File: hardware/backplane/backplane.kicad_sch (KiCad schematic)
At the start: 83 parts, among them J1 Bus_PCI_Express_x1, J2 PWR, J3 Bus_PCI_Express_x1, J4 Bus_PCI_Express_x1, J5 Bus_PCI_Express_x1, J6 Bus_PCI_Express_x1, J7 Bus_PCI_Express_x1, J8 Bus_PCI_Express_x1, M1 FAN1, Q1 IRFS7530TRL7PP, Q2 AO3400A, U1 TPS5430DDA, U2 TCA9548APWR, U3 TCA9539PWR, U4 LM74700

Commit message: chore: clean up socket definitions
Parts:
- J1, J3, J4, J5, J6, J7, J8: LCSC (none) -> C4693418; now not fitted
- U3: LCSC (none) -> C131972
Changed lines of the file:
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@@
 			)
 		)
+		(property "LCSC" "C131972"
+			(at 134.62 234.95 0)
+			(hide yes)
+			(show_name no)
+			(do_not_autoplace no)
+			(effects
+				(font
+					(size 1.27 1.27)
+				)
+			)
+		)
 		(pin "16"
 		)
@@
 		(on_board yes)
 		(in_pos_files yes)
-		(dnp no)
+		(dnp yes)
 		(fields_autoplaced yes)
 		(property "Reference" "J8"
@@
 			)
 		)
+		(property "LCSC" "C4693418"
+			(at 331.47 191.77 0)
+			(hide yes)
+			(show_name no)
+			(do_not_autoplace no)
+			(effects
+				(font
+					(size 1.27 1.27)
+				)
+			)
+		)
 		(pin "A10"
 		)
@@
 		(on_board yes)
 		(in_pos_files yes)
-		(dnp no)
+		(dnp yes)
 		(fields_autoplaced yes)
 		(property "Reference" "J1"
@@
 			)
 		)
+		(property "LCSC" "C4693418"
+			(at 62.23 166.37 0)
+			(hide yes)
+			(show_name no)
+			(do_not_autoplace no)
+			(effects
+				(font
+					(size 1.27 1.27)
+				)
+			)
+		)
 		(pin "A10"
 		)
@@
 		(on_board yes)
 		(in_pos_files yes)
-		(dnp no)
+		(dnp yes)
 		(fields_autoplaced yes)
 		(property "Reference" "J5"
@@
 			)
 		)
+		(property "LCSC" "C4693418"
+			(at 274.32 113.03 0)
+			(hide yes)
+			(show_name no)
+			(do_not_autoplace no)
+			(effects
+				(font
+					(size 1.27 1.27)
+				)
+			)
+		)
 		(pin "A10"
 		)
@@
 		(on_board yes)
 		(in_pos_files yes)
-		(dnp no)
+		(dnp yes)
 		(fields_autoplaced yes)
 		(property "Reference" "J7"
@@
 			)
 		)
+		(property "LCSC" "C4693418"
+			(at 331.47 114.3 0)
+			(hide yes)
+			(show_name no)
+			(do_not_autoplace no)
+			(effects
+				(font
+					(size 1.27 1.27)
+				)
+			)
+		)
 		(pin "A10"
 		)
@@
 		(on_board yes)
 		(in_pos_files yes)
-		(dnp no)
+		(dnp yes)
 		(fields_autoplaced yes)
 		(property "Reference" "J3"
@@
 			)
 		)
-		(property "Manufacturer_Name" ""
-			(at 217.17 111.76 0)
-			(hide yes)
-			(show_name no)
-			(do_not_autoplace no)
-			(effects
-				(font
-					(size 1.27 1.27)
-				)
-			)
-		)
-		(property "Manufacturer_Part_Number" ""
-			(at 217.17 111.76 0)
-			(hide yes)
-			(show_name no)
-			(do_not_autoplace no)
-			(effects
-				(font
-					(size 1.27 1.27)
-				)
-			)
-		)
-		(property "Mouser Part Number" ""
-			(at 217.17 111.76 0)
-			(hide yes)
-			(show_name no)
-			(do_not_autoplace no)
-			(effects
-				(font
-					(size 1.27 1.27)
-				)
-			)
-		)
-		(property "Mouser Price/Stock" ""
+		(property "LCSC" "C4693418"
 			(at 217.17 111.76 0)
 			(hide yes)
@@
 		(on_board yes)
 		(in_pos_files yes)
-		(dnp no)
+		(dnp yes)
 		(fields_autoplaced yes)
 		(property "Reference" "J4"
@@
 			)
 		)
+		(property "LCSC" "C4693418"
+			(at 217.17 189.23 0)
+			(hide yes)
+			(show_name no)
+			(do_not_autoplace no)
+			(effects
+				(font
+					(size 1.27 1.27)
+				)
+			)
+		)
 		(pin "A10"
 		)
@@
 		(on_board yes)
 		(in_pos_files yes)
-		(dnp no)
+		(dnp yes)
 		(fields_autoplaced yes)
 		(property "Reference" "J6"
@@
 			(at 274.32 190.5 0)
 			(hide yes)
+			(show_name no)
+			(do_not_autoplace no)
+			(effects
+				(font
+					(size 1.27 1.27)
+				)
+			)
+		)
+		(property "LCSC" "C4693418"
+			(at 274.32 190.5 0)
+			(hide yes)

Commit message: chore: remove DNP from sockets
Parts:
- J1, J3, J4, J5, J6, J7, J8: now fitted
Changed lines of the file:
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@@
 		(on_board yes)
 		(in_pos_files yes)
-		(dnp yes)
+		(dnp no)
 		(fields_autoplaced yes)
 		(property "Reference" "J8"
@@
 		(on_board yes)
 		(in_pos_files yes)
-		(dnp yes)
+		(dnp no)
 		(fields_autoplaced yes)
 		(property "Reference" "J1"
@@
 		(on_board yes)
 		(in_pos_files yes)
-		(dnp yes)
+		(dnp no)
 		(fields_autoplaced yes)
 		(property "Reference" "J5"
@@
 		(on_board yes)
 		(in_pos_files yes)
-		(dnp yes)
+		(dnp no)
 		(fields_autoplaced yes)
 		(property "Reference" "J7"
@@
 		(on_board yes)
 		(in_pos_files yes)
-		(dnp yes)
+		(dnp no)
 		(fields_autoplaced yes)
 		(property "Reference" "J3"
@@
 		(on_board yes)
 		(in_pos_files yes)
-		(dnp yes)
+		(dnp no)
 		(fields_autoplaced yes)
 		(property "Reference" "J4"
@@
 		(on_board yes)
 		(in_pos_files yes)
-		(dnp yes)
+		(dnp no)
 		(fields_autoplaced yes)
 		(property "Reference" "J6"

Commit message: chore(backplane): fix 3d models
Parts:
- D10, D5, D6, D7, D8, D9: footprint LED_SMD:LED_WS2812B-2020_PLCC4_2.0x2.0mm -> Local Library:LED_WS2812B-2020_PLCC4_2.0x2.0mm
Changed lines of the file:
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@@
 			)
 		)
-		(property "Footprint" "LED_SMD:LED_WS2812B-2020_PLCC4_2.0x2.0mm"
+		(property "Footprint" "Local Library:LED_WS2812B-2020_PLCC4_2.0x2.0mm"
 			(at 375.92 73.66 0)
 			(hide yes)
@@
 			)
 		)
-		(property "Footprint" "LED_SMD:LED_WS2812B-2020_PLCC4_2.0x2.0mm"
+		(property "Footprint" "Local Library:LED_WS2812B-2020_PLCC4_2.0x2.0mm"
 			(at 375.92 58.42 0)
 			(hide yes)
@@
 		(in_bom no)
 		(on_board yes)
-		(in_pos_files yes)
+		(in_pos_files no)
 		(dnp no)
 		(property "Reference" "F1"
@@
 			)
 		)
-		(property "Footprint" "LED_SMD:LED_WS2812B-2020_PLCC4_2.0x2.0mm"
+		(property "Footprint" "Local Library:LED_WS2812B-2020_PLCC4_2.0x2.0mm"
 			(at 375.92 134.62 0)
 			(hide yes)
@@
 			)
 		)
-		(property "Footprint" "LED_SMD:LED_WS2812B-2020_PLCC4_2.0x2.0mm"
+		(property "Footprint" "Local Library:LED_WS2812B-2020_PLCC4_2.0x2.0mm"
 			(at 375.92 119.38 0)
 			(hide yes)
@@
 		(in_bom no)
 		(on_board yes)
-		(in_pos_files yes)
+		(in_pos_files no)
 		(dnp no)
 		(property "Reference" "H1"
@@
 			)
 		)
-		(property "Footprint" "LED_SMD:LED_WS2812B-2020_PLCC4_2.0x2.0mm"
+		(property "Footprint" "Local Library:LED_WS2812B-2020_PLCC4_2.0x2.0mm"
 			(at 375.92 104.14 0)
 			(hide yes)
@@
 			)
 		)
-		(property "Footprint" "LED_SMD:LED_WS2812B-2020_PLCC4_2.0x2.0mm"
+		(property "Footprint" "Local Library:LED_WS2812B-2020_PLCC4_2.0x2.0mm"
 			(at 375.92 88.9 0)
 			(hide yes)
@@
 		(in_bom no)
 		(on_board yes)
-		(in_pos_files yes)
+		(in_pos_files no)
 		(dnp no)
 		(fields_autoplaced yes)

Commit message: chore: assembly cleanup
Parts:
- D10, D5, D6, D7, D8, D9: value WS2812C-2020 -> WS2812C-2020-V6
- J2: JLCPCB_CORRECTION (none) -> 3;1.5;180
- Q1: JLCPCB_CORRECTION -2.5;0;0 -> (none)
- Q2: JLCPCB_CORRECTION (none) -> 0;0;180
- RN1, RN2, RN3, RN4, RN5, RN6, RN7, RN8: JLCPCB_CORRECTION (none) -> 0;0;90
- U3, U4: JLCPCB_CORRECTION (none) -> 0;0;270
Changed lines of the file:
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@@
 			)
 		)
+		(property "JLCPCB_CORRECTION" "0;0;270"
+			(at 134.62 234.95 0)
+			(hide yes)
+			(show_name no)
+			(do_not_autoplace no)
+			(effects
+				(font
+					(size 1.27 1.27)
+				)
+			)
+		)
 		(pin "16"
 		)
@@
 			)
 		)
+		(property "JLCPCB_CORRECTION" "0;0;90"
+			(at 157.48 219.71 90)
+			(hide yes)
+			(show_name no)
+			(do_not_autoplace no)
+			(effects
+				(font
+					(size 1.27 1.27)
+				)
+			)
+		)
 		(pin "7"
 		)
@@
 			)
 		)
-		(property "Value" "WS2812C-2020"
+		(property "Value" "WS2812C-2020-V6"
 			(at 397.51 68.5098 90)
 			(show_name no)
@@
 			)
 		)
-		(property "Value" "WS2812C-2020"
+		(property "Value" "WS2812C-2020-V6"
 			(at 397.51 53.2698 90)
 			(show_name no)
@@
 			)
 		)
+		(property "JLCPCB_CORRECTION" "0;0;270"
+			(at 142.24 48.26 0)
+			(hide yes)
+			(show_name no)
+			(do_not_autoplace no)
+			(effects
+				(font
+					(size 1.27 1.27)
+				)
+			)
+		)
 		(pin "1"
 		)
@@
 			)
 		)
+		(property "JLCPCB_CORRECTION" "0;0;90"
+			(at 59.69 254 90)
+			(hide yes)
+			(show_name no)
+			(do_not_autoplace no)
+			(effects
+				(font
+					(size 1.27 1.27)
+				)
+			)
+		)
 		(pin "7"
 		)
@@
 			)
 		)
+		(property "JLCPCB_CORRECTION" "0;0;90"
+			(at 59.69 218.44 90)
+			(hide yes)
+			(show_name no)
+			(do_not_autoplace no)
+			(effects
+				(font
+					(size 1.27 1.27)
+				)
+			)
+		)
 		(pin "7"
 		)
@@
 			)
 		)
-		(property "JLCPCB_CORRECTION" "-2.5;0;0"
+		(property "JLCPCB_CORRECTION" ""
 			(at 142.24 31.75 90)
 			(hide yes)
@@
 			)
 		)
+		(property "JLCPCB_CORRECTION" "0;0;90"
+			(at 59.69 241.3 90)
+			(hide yes)
+			(show_name no)
+			(do_not_autoplace no)
+			(effects
+				(font
+					(size 1.27 1.27)
+				)
+			)
+		)
 		(pin "7"
 		)
@@
 			)
 		)
+		(property "JLCPCB_CORRECTION" "0;0;180"
+			(at 194.31 45.72 0)
+			(hide yes)
+			(show_name no)
+			(do_not_autoplace no)
+			(effects
+				(font
+					(size 1.27 1.27)
+				)
+			)
+		)
 		(pin "1"
 		)
@@
 			)
 		)
-		(property "Value" "WS2812C-2020"
+		(property "Value" "WS2812C-2020-V6"
 			(at 397.51 129.4698 90)
 			(show_name no)
@@
 			)
 		)
-		(property "Value" "WS2812C-2020"
+		(property "Value" "WS2812C-2020-V6"
 			(at 397.51 114.2298 90)
 			(show_name no)
@@
 			)
 		)
+		(property "JLCPCB_CORRECTION" "0;0;90"
+			(at 157.48 242.57 90)
+			(hide yes)
+			(show_name no)
+			(do_not_autoplace no)
+			(effects
+				(font
+					(size 1.27 1.27)
+				)
+			)
+		)
 		(pin "7"
 		)
@@
 			)
 		)
-		(property "Value" "WS2812C-2020"
+		(property "Value" "WS2812C-2020-V6"
 			(at 397.51 98.9898 90)
 			(show_name no)
@@
 			)
 		)
+		(property "JLCPCB_CORRECTION" "0;0;90"
+			(at 59.69 228.6 90)
+			(hide yes)
+			(show_name no)
+			(do_not_autoplace no)
+			(effects
+				(font
+					(size 1.27 1.27)
+				)
+			)
+		)
 		(pin "7"
 		)
@@
 			)
 		)
+		(property "JLCPCB_CORRECTION" "0;0;90"
+			(at 157.48 252.73 90)
+			(hide yes)
+			(show_name no)
+			(do_not_autoplace no)
+			(effects
+				(font
+					(size 1.27 1.27)
+				)
+			)
+		)
 		(pin "7"
 		)
@@
 			)
 		)
+		(property "JLCPCB_CORRECTION" "0;0;90"
+			(at 157.48 229.87 90)
+			(hide yes)
+			(show_name no)
+			(do_not_autoplace no)
+			(effects
+				(font
+					(size 1.27 1.27)
+				)
+			)
+		)
 		(pin "7"
 		)
@@
 			)
 		)
-		(property "Value" "WS2812C-2020"
+		(property "Value" "WS2812C-2020-V6"
 			(at 397.51 83.7498 90)
 			(show_name no)
@@
 			(at 78.74 36.83 90)
 			(hide yes)
+			(show_name no)
+			(do_not_autoplace no)
+			(effects
+				(font
+					(size 1.27 1.27)
+				)
+			)
+		)
+		(property "JLCPCB_CORRECTION" "3;1.5;180"
+			(at 78.74 36.83 90)
+			(hide yes)

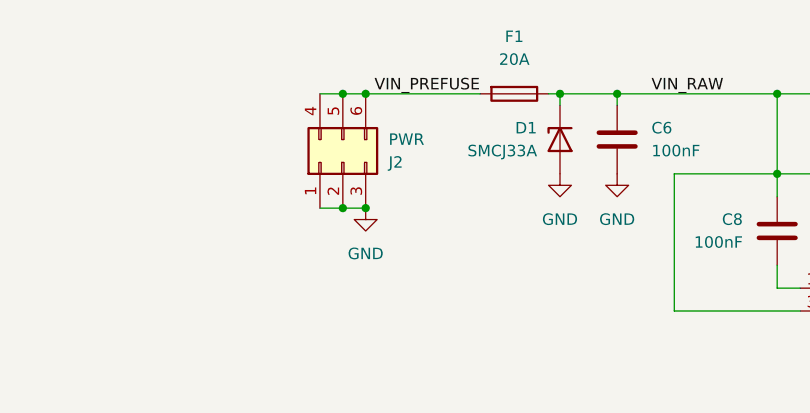
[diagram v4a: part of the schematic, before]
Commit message: feat(backplane): update pcb for higher power
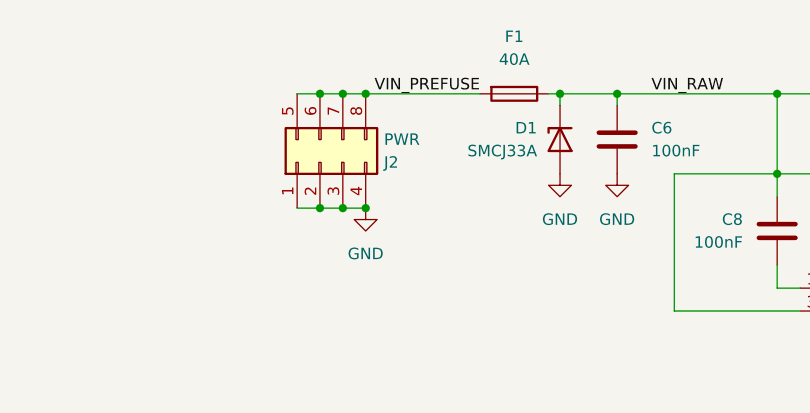
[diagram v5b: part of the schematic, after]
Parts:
- F1: value 20A -> 40A; footprint Local Library:Fuseholder_Blade_Mini_Keystone_3568 -> Local Library:FuseHolder_Blade_ATO_Littelfuse_FLR_178.6165
- J2: footprint Local Library:Molex_Micro-Fit_3.0_43045-0600_2x03_P3.00mm_Horizontal -> Local Library:Molex_Micro-Fit_3.0_43045-0812_2x04_P3.00mm_Vertical; symbol Connector_Generic:Conn_02x03_Top_Bottom -> Connector_Generic:Conn_02x04_Top_Bottom; JLCPCB_CORRECTION 3;1.5;180 -> 0;0;0; LCSC C3294384 -> C505221
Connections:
- net GND: now also J2.4 (Pin_4)
- net VIN_PREFUSE: now also J2.7 (Pin_7), J2.8 (Pin_8); no longer J2.4 (Pin_4)
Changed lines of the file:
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@@
 	)
 	(junction
-		(at 78.74 29.21)
+		(at 220.98 154.94)
 		(diameter 0)
 		(color 0 0 0 0)
 	)
 	(junction
-		(at 220.98 154.94)
+		(at 233.68 77.47)
 		(diameter 0)
 		(color 0 0 0 0)
 	)
 	(junction
-		(at 233.68 77.47)
+		(at 393.7 57.15)
 		(diameter 0)
 		(color 0 0 0 0)
 	)
 	(junction
-		(at 393.7 57.15)
+		(at 76.2 29.21)
 		(diameter 0)
 		(color 0 0 0 0)
@@
 	)
 	(junction
+		(at 78.74 29.21)
+		(diameter 0)
+		(color 0 0 0 0)
+	)
+	(junction
 		(at 278.13 78.74)
 		(diameter 0)
@@
 	)
 	(junction
-		(at 401.32 92.71)
+		(at 81.28 41.91)
 		(diameter 0)
 		(color 0 0 0 0)
 	)
 	(junction
-		(at 347.98 80.01)
+		(at 401.32 92.71)
 		(diameter 0)
 		(color 0 0 0 0)
 	)
 	(junction
-		(at 217.17 134.62)
+		(at 347.98 80.01)
 		(diameter 0)
 		(color 0 0 0 0)
 	)
 	(junction
-		(at 81.28 41.91)
+		(at 217.17 134.62)
 		(diameter 0)
 		(color 0 0 0 0)
@@
 	)
 	(junction
+		(at 78.74 41.91)
+		(diameter 0)
+		(color 0 0 0 0)
+	)
+	(junction
 		(at 111.76 109.22)
 		(diameter 0)
@@
 	)
 	(junction
-		(at 81.28 29.21)
+		(at 64.77 218.44)
 		(diameter 0)
 		(color 0 0 0 0)
 	)
 	(junction
-		(at 64.77 218.44)
+		(at 76.2 41.91)
 		(diameter 0)
 		(color 0 0 0 0)
@@
 	)
 	(junction
+		(at 81.28 29.21)
+		(diameter 0)
+		(color 0 0 0 0)
+	)
+	(junction
 		(at 393.7 92.71)
 		(diameter 0)
@@
 	)
 	(junction
-		(at 78.74 41.91)
-		(diameter 0)
-		(color 0 0 0 0)
-	)
-	(junction
 		(at 393.7 60.96)
 		(diameter 0)
@@
 	(wire
 		(pts
-			(xy 76.2 41.91) (xy 78.74 41.91)
+			(xy 73.66 41.91) (xy 76.2 41.91)
 		)
 		(stroke
@@
 	(wire
 		(pts
+			(xy 76.2 29.21) (xy 78.74 29.21)
+		)
+		(stroke
+			(width 0)
+			(type default)
+		)
+	)
+	(wire
+		(pts
 			(xy 120.65 171.45) (xy 120.65 173.99)
 		)
@@
 	(wire
 		(pts
-			(xy 76.2 29.21) (xy 78.74 29.21)
+			(xy 73.66 29.21) (xy 76.2 29.21)
 		)
 		(stroke
@@
 	(wire
 		(pts
+			(xy 76.2 41.91) (xy 78.74 41.91)
+		)
+		(stroke
+			(width 0)
+			(type default)
+		)
+	)
+	(wire
+		(pts
 			(xy 116.84 262.89) (xy 134.62 262.89)
 		)
@@
 	(wire
 		(pts
-			(xy 78.74 41.91) (xy 81.28 41.91)
-		)
-		(stroke
-			(width 0)
-			(type default)
-		)
-	)
-	(wire
-		(pts
 			(xy 393.7 57.15) (xy 393.7 60.96)
 		)
@@
 	(wire
 		(pts
+			(xy 78.74 41.91) (xy 81.28 41.91)
+		)
+		(stroke
+			(width 0)
+			(type default)
+		)
+	)
+	(wire
+		(pts
 			(xy 116.84 255.27) (xy 116.84 262.89)
 		)
@@
 			)
 		)
-		(property "Value" "20A"
+		(property "Value" "40A"
 			(at 97.79 25.4 90)
 			(show_name no)
@@
 			)
 		)
-		(property "Footprint" "Local Library:Fuseholder_Blade_Mini_Keystone_3568"
+		(property "Footprint" "Local Library:FuseHolder_Blade_ATO_Littelfuse_FLR_178.6165"
 			(at 97.79 27.432 90)
 			(hide yes)
@@
 	)
 	(symbol
-		(lib_id "Connector_Generic:Conn_02x03_Top_Bottom")
-		(at 78.74 36.83 90)
+		(lib_id "Connector_Generic:Conn_02x04_Top_Bottom")
+		(at 76.2 36.83 90)
 		(unit 1)
 		(body_style 1)
@@
 		(dnp no)
 		(property "Reference" "J2"
-			(at 83.82 36.8301 90)
+			(at 83.312 36.83 90)
 			(show_name no)
 			(do_not_autoplace no)
@@
 		)
 		(property "Value" "PWR"
-			(at 83.82 34.2901 90)
+			(at 83.312 34.29 90)
 			(show_name no)
 			(do_not_autoplace no)
@@
 			)
 		)
-		(property "Footprint" "Local Library:Molex_Micro-Fit_3.0_43045-0600_2x03_P3.00mm_Horizontal"
-			(at 78.74 36.83 0)
+		(property "Footprint" "Local Library:Molex_Micro-Fit_3.0_43045-0812_2x04_P3.00mm_Vertical"
+			(at 76.2 36.83 0)
 			(hide yes)
 			(show_name no)
@@
 		)
 		(property "Datasheet" ""
-			(at 78.74 36.83 0)
+			(at 76.2 36.83 0)
 			(hide yes)
 			(show_name no)
@@
 			)
 		)
-		(property "Description" "Generic connector, double row, 02x03, top/bottom pin numbering scheme (row 1: 1...pins_per_row, row2: pins_per_row+1 ... num_pins), script generated (kicad-library-utils/schlib/autogen/connector/)"
-			(at 78.74 36.83 0)
+		(property "Description" "Generic connector, double row, 02x04, top/bottom pin numbering scheme (row 1: 1...pins_per_row, row2: pins_per_row+1 ... num_pins), script generated (kicad-library-utils/schlib/autogen/connector/)"
+			(at 76.2 36.83 0)
 			(hide yes)
 			(show_name no)
@@
 			)
 		)
-		(property "LCSC" "C3294384"
-			(at 78.74 36.83 90)
+		(property "LCSC" "C505221"
+			(at 76.2 36.83 90)
 			(hide yes)
 			(show_name no)
@@
 			)
 		)
-		(property "JLCPCB_CORRECTION" "3;1.5;180"
-			(at 78.74 36.83 90)
+		(property "JLCPCB_CORRECTION" "0;0;0"
+			(at 76.2 36.83 90)
 			(hide yes)
 			(show_name no)
@@
 		(pin "3"
 		)
+		(pin "7"
+		)
+		(pin "8"
+		)
 		(instances
